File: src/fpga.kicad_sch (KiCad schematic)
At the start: 25 parts

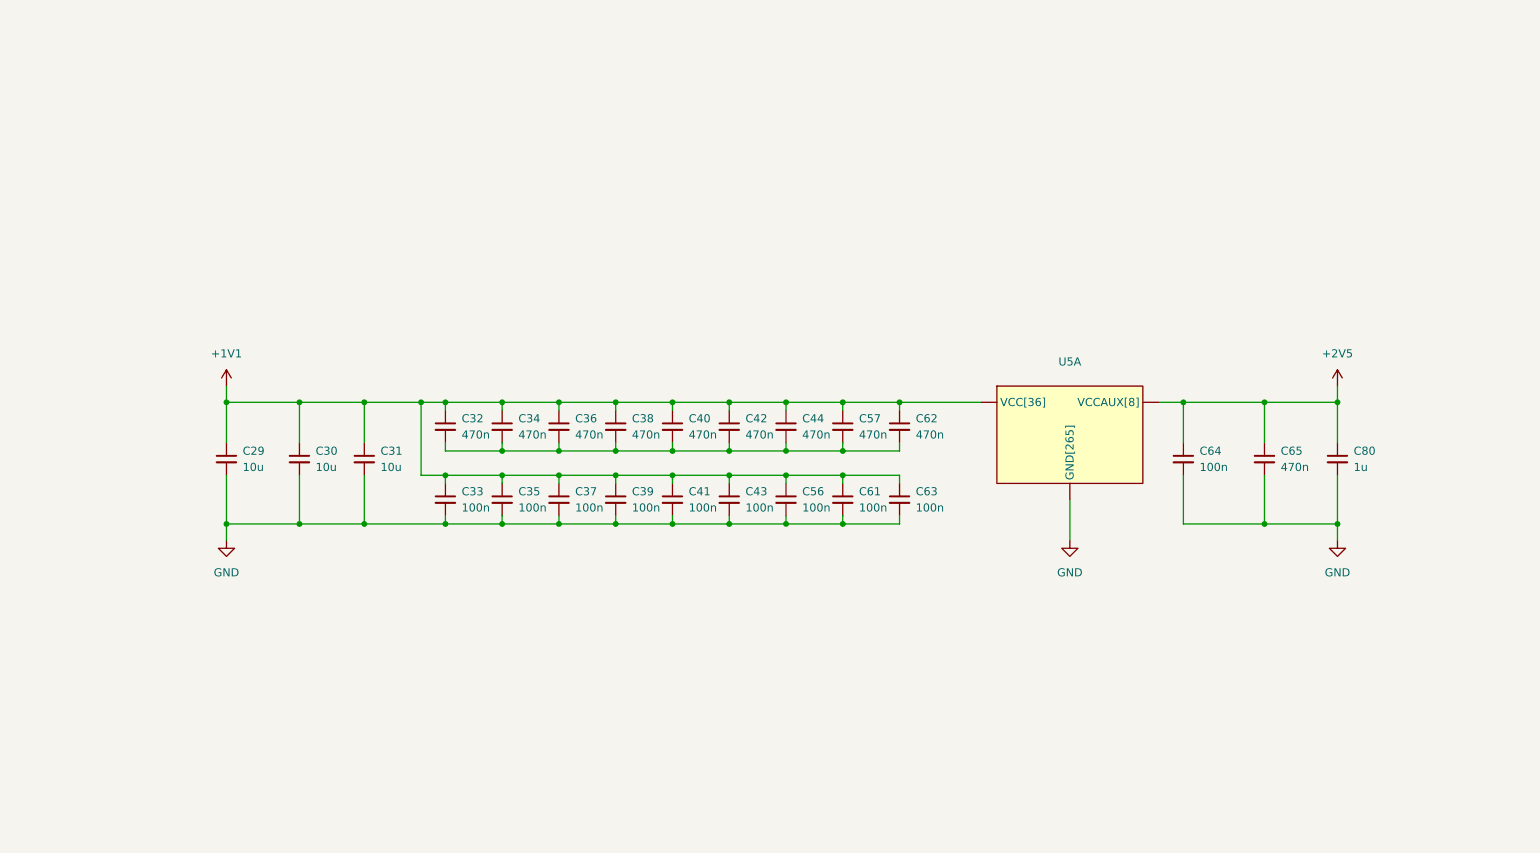
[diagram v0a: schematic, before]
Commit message: Updates the structure of the schematic
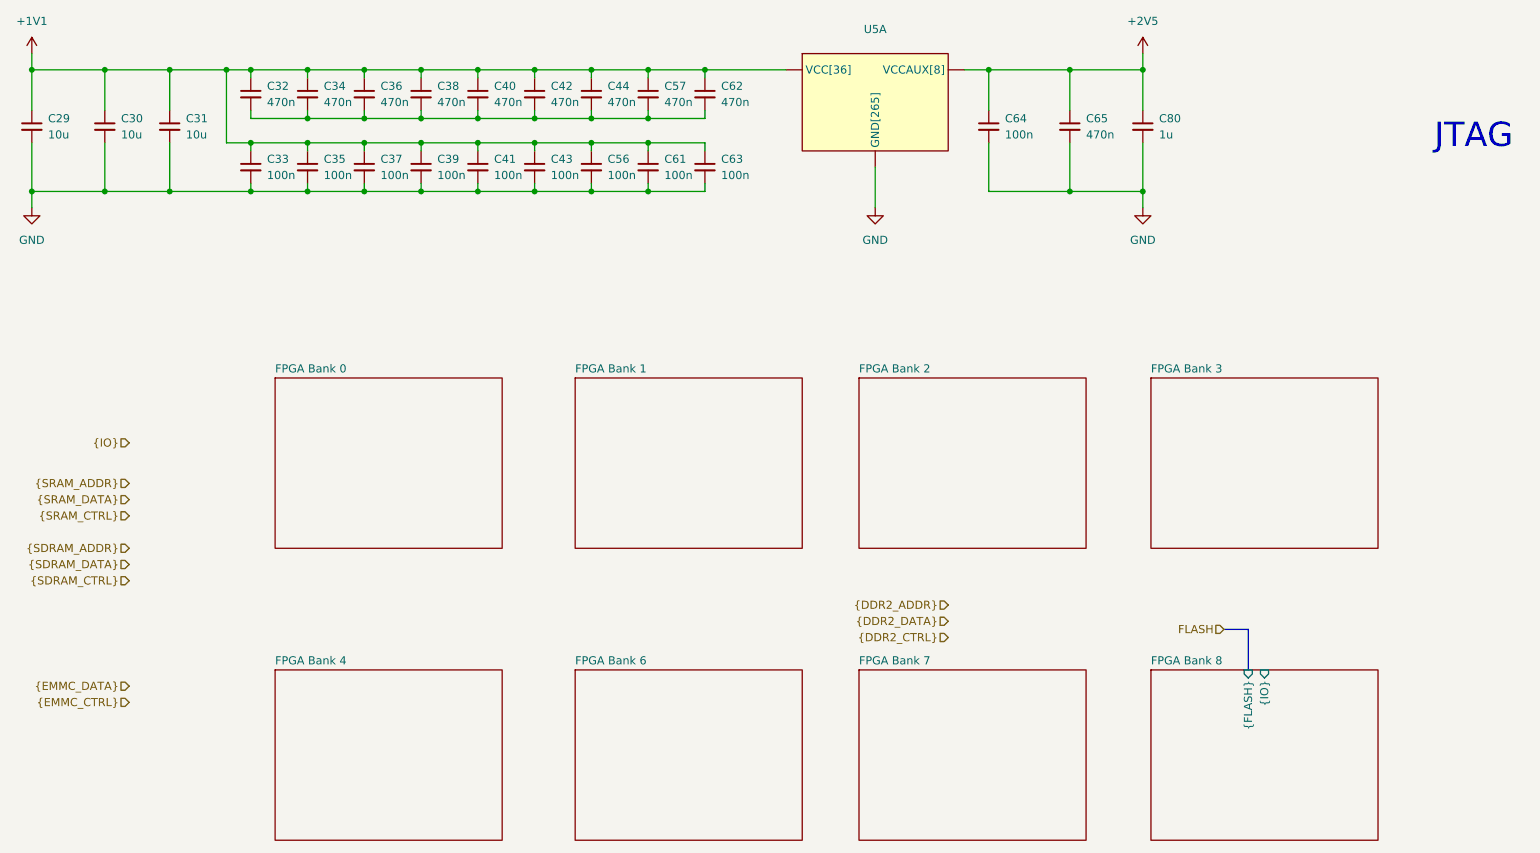
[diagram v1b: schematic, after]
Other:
- added sheet FPGA Bank 0 (fpga-bank0.kicad_sch)
- added sheet FPGA Bank 1 (fpga-bank1.kicad_sch)
- added sheet FPGA Bank 2 (fpga-bank2.kicad_sch)
- added sheet FPGA Bank 3 (fpga-bank3.kicad_sch)
- added sheet FPGA Bank 4 (fpga-bank4.kicad_sch)
- added sheet FPGA Bank 6 (fpga-bank6.kicad_sch)
- added sheet FPGA Bank 7 (fpga-bank7.kicad_sch)
- added sheet FPGA Bank 8 (fpga-bank8.kicad_sch)
- note added: "JTAG"
